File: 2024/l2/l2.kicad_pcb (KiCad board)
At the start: 2 copper layers, 175 x 169.4 mm, 45 parts, among them J1 Conn_01x04, J2 Conn_01x02, J3 Conn_01x04, Q1 IRF540N, Q2 IRF540N, Q3 IRF540N, Q4 IRF540N, SW1 SW_SPDT, U1 VNH5019A-E, U2 VNH5019A-E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

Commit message: 16/8 final
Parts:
- added H1: MountingHole_Pad, MountingHole:MountingHole_3.2mm_M3_Pad_Via, F.Cu at (245.0, 118.0)
- added H10: MountingHole_Pad, MountingHole:MountingHole_3.2mm_M3_Pad_Via, F.Cu at (260.9, 126.0)
- added H11: MountingHole_Pad, MountingHole:MountingHole_3.2mm_M3_Pad_Via, F.Cu at (260.9, 133.9)
- added H12: MountingHole_Pad, MountingHole:MountingHole_3.2mm_M3_Pad_Via, F.Cu at (260.9, 141.9)
- added H13: MountingHole_Pad, MountingHole:MountingHole_3.2mm_M3_Pad_Via, F.Cu at (268.8, 118.0)
- added H14: MountingHole_Pad, MountingHole:MountingHole_3.2mm_M3_Pad_Via, F.Cu at (268.8, 126.0)
- added H15: MountingHole_Pad, MountingHole:MountingHole_3.2mm_M3_Pad_Via, F.Cu at (268.8, 133.9)
- added H16: MountingHole_Pad, MountingHole:MountingHole_3.2mm_M3_Pad_Via, F.Cu at (268.8, 141.9)
- added H2: MountingHole_Pad, MountingHole:MountingHole_3.2mm_M3_Pad_Via, F.Cu at (245.0, 126.0)
- added H3: MountingHole_Pad, MountingHole:MountingHole_3.2mm_M3_Pad_Via, F.Cu at (245.0, 133.9)
- added H4: MountingHole_Pad, MountingHole:MountingHole_3.2mm_M3_Pad_Via, F.Cu at (245.0, 141.9)
- added H5: MountingHole_Pad, MountingHole:MountingHole_3.2mm_M3_Pad_Via, F.Cu at (252.9, 118.0)
- added H6: MountingHole_Pad, MountingHole:MountingHole_3.2mm_M3_Pad_Via, F.Cu at (252.9, 126.0)
- added H7: MountingHole_Pad, MountingHole:MountingHole_3.2mm_M3_Pad_Via, F.Cu at (252.9, 133.9)
- added H8: MountingHole_Pad, MountingHole:MountingHole_3.2mm_M3_Pad_Via, F.Cu at (252.9, 141.9)
- added H9: MountingHole_Pad, MountingHole:MountingHole_3.2mm_M3_Pad_Via, F.Cu at (260.9, 118.0)
- C1, C2, C3, C4: footprint Capacitor_SMD:C_0603_1608Metric_Pad1.08x0.95mm_HandSolder -> Capacitor_THT:CP_Radial_D8.0mm_P3.50mm
- moved R8 16.8 mm to (168.7, 95.7), turned to 180 degrees
- moved R12 9.37 mm to (169.9, 98.2)
- moved R11 7.68 mm to (168.8, 94.0)
- moved R10 6.78 mm to (168.9, 90.7)
- moved R13 4.12 mm to (173.8, 89.9)
- moved R14 2.06 mm to (168.7, 92.4), turned to 180 degrees
- turned U1 to 180 degrees
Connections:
- R14 pad 1: /Motor Driver/PWM_1 -> PWM_1
- U5 pad 4: /PWM_1 -> PWM_1
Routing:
- net /Motor Driver/MD: track 0.00 -> 3.96 mm
- net Net-(U1-EN/DIAGB): track 0.00 -> 3.76 mm
- net Net-(U1-PWM): track 0.00 -> 3.66 mm

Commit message: 21/8 final
about 10% done l2 pcb
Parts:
- added J4: Conn_01x02, Connector_AMASS:AMASS_XT30UPB-F_1x02_P5.0mm_Vertical, F.Cu at (144.6, 97.0)
- added J5: Conn_01x02, Connector_AMASS:AMASS_XT30UPB-F_1x02_P5.0mm_Vertical, F.Cu at (190.2, 54.5)
- added J6: Conn_01x02, Connector_AMASS:AMASS_XT30UPB-F_1x02_P5.0mm_Vertical, F.Cu at (295.0, 78.4)
- added J7: Conn_01x02, Connector_AMASS:AMASS_XT30UPB-F_1x02_P5.0mm_Vertical, F.Cu at (295.0, 85.7)
- moved H1 136.5 mm to (125.1, 52.6)
- moved U5 67.3 mm to (319.1, 108.3)
- moved Q1 40.6 mm to (197.9, 75.4)
- moved C1 38.4 mm to (170.3, 123.8)
- moved R12 31.6 mm to (141.1, 85.3), turned to 90 degrees
- moved R8 27.9 mm to (142.8, 85.4), turned to 90 degrees
- moved R11 25.8 mm to (144.5, 85.4), turned to -90 degrees
- moved R14 23.7 mm to (146.1, 85.3), turned to 90 degrees
- moved R13 23.3 mm to (150.9, 85.6), turned to 90 degrees
- moved U1 21.9 mm to (146.5, 71.9), turned to 90 degrees
- moved R10 21.7 mm to (147.9, 85.5), turned to -90 degrees
- moved R9 21.0 mm to (149.4, 85.6), turned to 90 degrees
- moved J2 3.28 mm to (273.4, 64.8)
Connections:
- R12 pad 1: /Motor Driver/INA_1 -> INA_1
- R13 pad 1: /Motor Driver/INB_1 -> INB_1
- R19 pad 1: /Motor Driver/INA_3 -> INA_3
- R20 pad 1: /Motor Driver/INB_3 -> INB_3
- R21 pad 1: /Motor Driver/PWM_3 -> PWM_3
- R26 pad 1: /Motor Driver/INA_4 -> INA_4
- R27 pad 1: /Motor Driver/INB_4 -> INB_4
- R28 pad 1: /Motor Driver/PWM_4 -> PWM_4
- R5 pad 1: /Motor Driver/INA_2 -> INA_2
- R6 pad 1: /Motor Driver/INB_2 -> INB_2
- R7 pad 1: /Motor Driver/PWM_2 -> PWM_2
- U5 pad 10: /INA_3 -> INA_3
- U5 pad 11: /INB_3 -> INB_3
- U5 pad 12: /PWM_3 -> PWM_3
- U5 pad 13: /INA_3 -> INA_4
- U5 pad 14: /INB_3 -> INB_4
- U5 pad 15: /PWM_3 -> PWM_4
- U5 pad 2: /INA_1 -> INA_1
- U5 pad 3: /INB_1 -> INB_1
- U5 pad 5: /INA_2 -> INA_2
- U5 pad 6: /INB_2 -> INB_2
- U5 pad 9: /PWM_2 -> PWM_2
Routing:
- net Net-(J4-Pin_1): track 0.00 -> 18.1 mm
- net Net-(J4-Pin_2): track 0.00 -> 17.7 mm
- net Net-(U1-EN/DIAGA): track 0.00 -> 5.44 mm
- net Net-(U1-INB): track 0.00 -> 4.72 mm
- net Net-(U1-INA): track 0.00 -> 4.01 mm
- net /Motor Driver/MD: track 3.96 -> 6.76 mm
- net Net-(U1-EN/DIAGB): track 3.76 -> 5.34 mm

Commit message: 28/8 final
resistors for motor driver removed as it was too cumbersome to do the traces and is also completely optional
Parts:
- removed R1, R12, R13, R14, R15, R16, R19, R2, R20, R21, R22, R23, R26, R27, R28, R5, R6, R7, R8, R9: 1k, Resistor_SMD:R_0603_1608Metric_Pad0.98x0.95mm_HandSolder
- removed R10, R11, R17, R18, R24, R25, R3, R4: 3.3k, Resistor_SMD:R_0603_1608Metric_Pad0.98x0.95mm_HandSolder
- J4, J5, J6, J7: moved to B.Cu
- moved U5 277.1 mm to (42.1, 101.3), turned to 180 degrees
- moved H14 243.2 mm to (29.8, 81.3)
- moved H13 239.1 mm to (29.8, 123.3)
- moved J6 234.0 mm to (69.0, 139.2)
- moved H15 220.2 mm to (55.0, 81.2)
- moved H16 209.6 mm to (79.5, 52.1)
- moved H12 206.7 mm to (55.0, 123.4)
- moved H10 191.6 mm to (76.3, 177.2)
- moved H11 182.4 mm to (79.5, 152.6)
- moved J7 163.3 mm to (143.1, 145.6)
- moved C3 157.4 mm to (82.3, 139.3)
- moved Q3 154.2 mm to (88.6, 130.8)
- moved U2 147.9 mm to (73.2, 72.5), turned to 90 degrees
- moved Q2 147.6 mm to (86.5, 83.7)
- moved C2 146.3 mm to (86.5, 92.0), turned to 180 degrees
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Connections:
- SW1 pad 2: /Motor Driver/MD -> GND
- U1 pad 10: Net-(U1-INB) -> INB_1
- U1 pad 4: Net-(U1-INA) -> INA_1
- U1 pad 5: Net-(U1-EN/DIAGA) -> GND
- U1 pad 7: Net-(U1-PWM) -> PWM_1
- U1 pad 9: Net-(U1-EN/DIAGB) -> GND
- U2 pad 10: Net-(U2-INB) -> INB_2
- U2 pad 4: Net-(U2-INA) -> INA_2
- U2 pad 5: Net-(U2-EN/DIAGA) -> GND
- U2 pad 7: Net-(U2-PWM) -> PWM_2
- U2 pad 9: Net-(U2-EN/DIAGB) -> GND
- U3 pad 10: Net-(U3-INB) -> INB_3
- U3 pad 4: Net-(U3-INA) -> INA_3
- U3 pad 5: Net-(U3-EN/DIAGA) -> GND
- U3 pad 7: Net-(U3-PWM) -> PWM_3
- U3 pad 9: Net-(U3-EN/DIAGB) -> GND
- U4 pad 10: Net-(U4-INB) -> INB_4
- U4 pad 4: Net-(U4-INA) -> INA_4
- U4 pad 5: Net-(U4-EN/DIAGA) -> GND
- U4 pad 7: Net-(U4-PWM) -> PWM_4
- U4 pad 9: Net-(U4-EN/DIAGB) -> GND
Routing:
- net Net-(J4-Pin_1): track 18.1 -> 0.00 mm
- net Net-(J4-Pin_2): track 17.7 -> 0.00 mm
- net /Motor Driver/MD: track 6.76 -> 0.00 mm
- net Net-(U1-EN/DIAGA): track 5.44 -> 0.00 mm
- net Net-(U1-EN/DIAGB): track 5.34 -> 0.00 mm
- net Net-(U1-INB): track 4.72 -> 0.00 mm
- net Net-(U1-INA): track 4.01 -> 0.00 mm
- net Net-(U1-PWM): track 3.66 -> 0.00 mm

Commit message: 4/9 final
some cursed motor driver routing
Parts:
- moved U5 186.0 mm to (222.7, 146.3)
- moved C3 184.0 mm to (263.9, 168.9)
- moved J6 184.0 mm to (250.7, 168.8)
- moved Q3 184.0 mm to (270.2, 160.4)
- moved U3 184.0 mm to (254.5, 147.5)
- moved C2 156.5 mm to (234.9, 42.3)
- moved J5 156.5 mm to (219.0, 37.4)
- moved U2 156.5 mm to (221.6, 22.9)
- moved Q2 156.5 mm to (234.9, 34.0)
- moved J7 107.6 mm to (227.3, 78.6)
- moved C4 107.6 mm to (240.8, 78.2)
- moved Q4 107.6 mm to (253.3, 47.9)
- moved U4 107.6 mm to (231.8, 60.7)
- moved J4 34.1 mm to (121.4, 71.3), turned to 45 degrees
- moved C1 29.4 mm to (162.3, 67.8), turned to -45 degrees
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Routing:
- net GND: track 0.00 -> 6.83 mm, vias 0 -> 2
- net /Motor Driver/CP: track 0.00 -> 0.51 mm
- added copper zone on F.Cu, net +5V
- added copper zone on F.Cu, net Net-(J4-Pin_1)
- added copper zone on F.Cu, net Net-(J4-Pin_2)

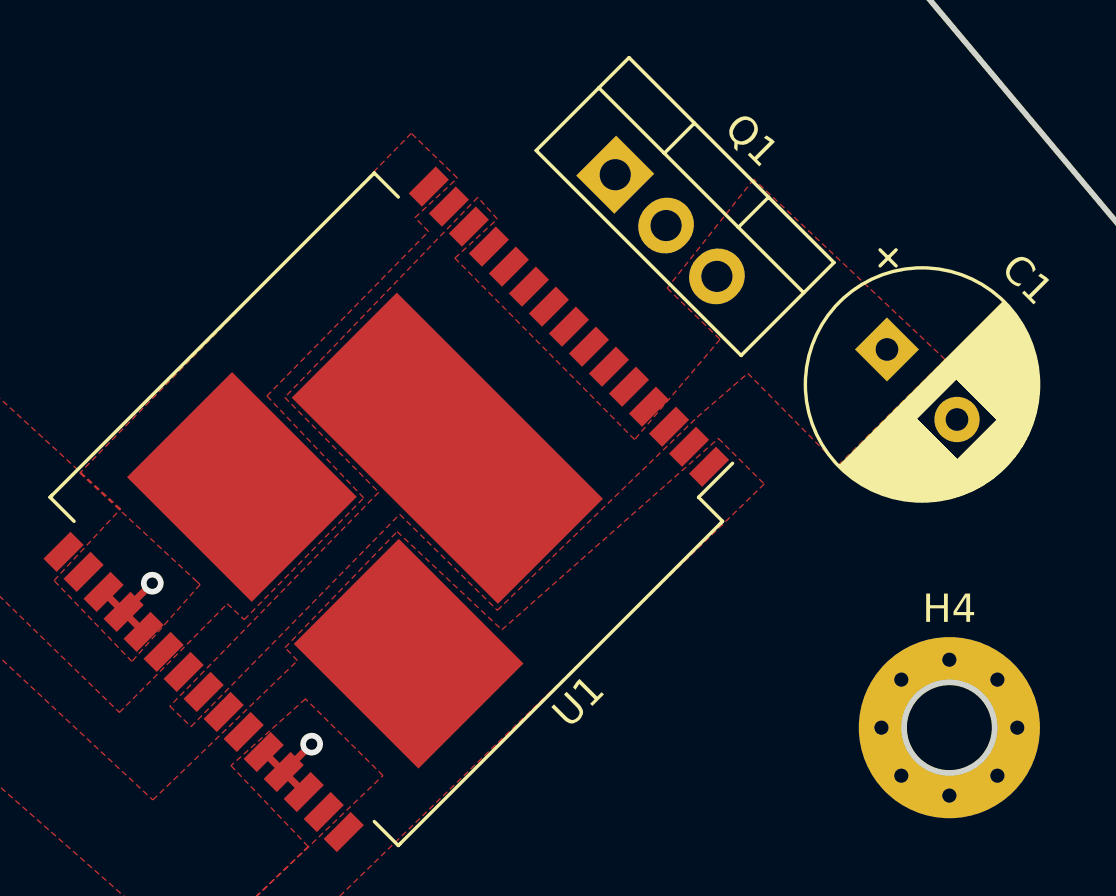
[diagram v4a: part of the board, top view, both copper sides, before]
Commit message: 5/9 final
fixed the problem with motor driver schematics
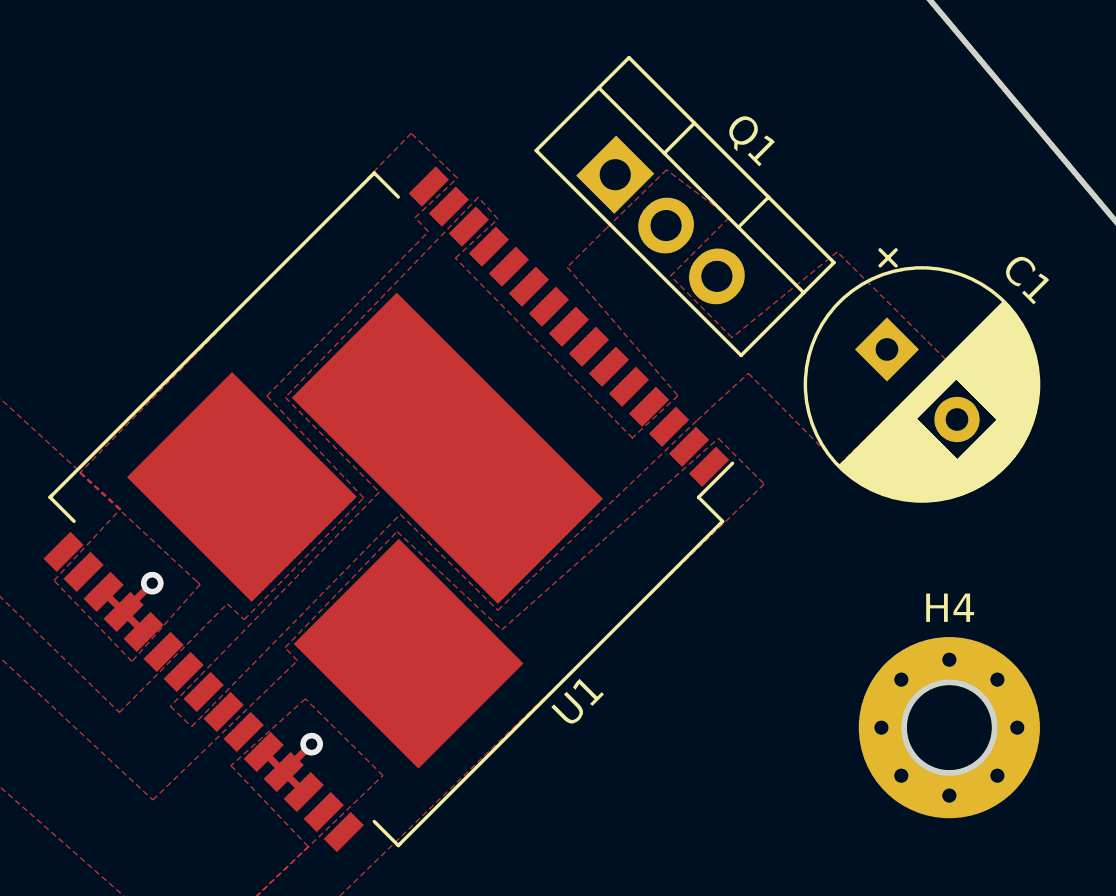
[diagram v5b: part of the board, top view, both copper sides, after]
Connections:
- C1 pad 1: +5V -> Net-(Q1-D)
- C2 pad 1: +5V -> Net-(Q2-D)
- C3 pad 1: +5V -> Net-(Q3-D)
- C4 pad 1: +5V -> Net-(Q4-D)
- Q1 pad 1: /Motor Driver/CP -> /Motor Driver/CP1
- Q1 pad 2: +12V -> Net-(Q1-D)
- Q1 pad 3: +5V -> +12V
- Q2 pad 1: /Motor Driver/CP -> /Motor Driver/CP2
- Q2 pad 2: +12V -> Net-(Q2-D)
- Q2 pad 3: +5V -> +12V
- Q3 pad 1: /Motor Driver/CP -> /Motor Driver/CP3
- Q3 pad 2: +12V -> Net-(Q3-D)
- Q3 pad 3: +5V -> +12V
- Q4 pad 1: /Motor Driver/CP -> /Motor Driver/CP4
- Q4 pad 2: +12V -> Net-(Q4-D)
- Q4 pad 3: +5V -> +12V
- SW1 pad 2: GND -> /Motor Driver/MD
- U1 pad 11: /Motor Driver/CP -> /Motor Driver/CP1
- U1 pad 13: +5V -> Net-(Q1-D)
- U1 pad 23: +5V -> Net-(Q1-D)
- U1 pad 3: +5V -> Net-(Q1-D)
- U1 pad 31: +5V -> Net-(Q1-D)
- U1 pad 5: GND -> /Motor Driver/MD
- U1 pad 9: GND -> /Motor Driver/MD
- U2 pad 11: /Motor Driver/CP -> /Motor Driver/CP2
- U2 pad 13: +5V -> Net-(Q2-D)
- U2 pad 23: +5V -> Net-(Q2-D)
- U2 pad 3: +5V -> Net-(Q2-D)
- U2 pad 31: +5V -> Net-(Q2-D)
- U2 pad 5: GND -> /Motor Driver/MD
- U2 pad 9: GND -> /Motor Driver/MD
- U3 pad 11: /Motor Driver/CP -> /Motor Driver/CP3
- U3 pad 13: +5V -> Net-(Q3-D)
- U3 pad 23: +5V -> Net-(Q3-D)
- U3 pad 3: +5V -> Net-(Q3-D)
- U3 pad 31: +5V -> Net-(Q3-D)
- U3 pad 5: GND -> /Motor Driver/MD
- U3 pad 9: GND -> /Motor Driver/MD
- U4 pad 11: /Motor Driver/CP -> /Motor Driver/CP4
- U4 pad 13: +5V -> Net-(Q4-D)
- U4 pad 23: +5V -> Net-(Q4-D)
- U4 pad 3: +5V -> Net-(Q4-D)
- U4 pad 31: +5V -> Net-(Q4-D)
- U4 pad 5: GND -> /Motor Driver/MD
- U4 pad 9: GND -> /Motor Driver/MD
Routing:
- net /Motor Driver/CP1: track 0.00 -> 0.51 mm
- net /Motor Driver/CP: track 0.51 -> 0.00 mm

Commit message: edited motor driver pcb
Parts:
- moved U5 129.8 mm to (301.6, 43.2)
- moved J2 94.2 mm to (188.3, 105.2), turned to 90 degrees
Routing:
- net +12V: track 0.00 -> 176.9 mm
- net /Motor Driver/MD: track 0.00 -> 5.94 mm
- net /Motor Driver/CP1: track 0.51 -> 5.10 mm
- added copper zone on F.Cu, net +12V
- added copper zone on F.Cu, net Net-(Q1-D)
- removed copper zone on F.Cu, net +5V
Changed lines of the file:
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@@
 	(footprint "Connector_AMASS:AMASS_XT60-M_1x02_P7.20mm_Vertical"
 		(layer "F.Cu")
-		(at 273.43 64.84)
+		(at 188.32 105.16 90)
 		(descr "AMASS female XT60, through hole, vertical, https://www.tme.eu/Document/2d152ced3b7a446066e6c419d84bb460/XT60%20SPEC.pdf")
 		(tags "XT60 female vertical")
 		(property "Reference" "J2"
-			(at 3.6 -5.3 180)
+			(at 3.599999 -5.3 90)
 			(layer "F.SilkS")
 			(effects
@@
 		)
 		(property "Value" "Conn_01x02"
-			(at 3.6 5.4 0)
+			(at 3.6 5.4 90)
 			(layer "F.Fab")
 			(effects
@@
 		)
 		(property "Footprint" "Connector_AMASS:AMASS_XT60-M_1x02_P7.20mm_Vertical"
-			(at 0 0 0)
+			(at 0 0 90)
 			(layer "F.Fab")
 			(hide yes)
@@
 		)
 		(property "Datasheet" ""
-			(at 0 0 0)
+			(at 0 0 90)
 			(layer "F.Fab")
 			(hide yes)
@@
 		)
 		(property "Description" ""
-			(at 0 0 0)
+			(at 0 0 90)
 			(layer "F.Fab")
 			(hide yes)
@@
 		(attr through_hole)
 		(fp_line
-			(start -4.25 -1.6)
-			(end -4.25 1.55)
+			(start -1.4 -4.150001)
+			(end -4.25 -1.6)
 			(stroke
 				(width 0.12)
@@
 		)
 		(fp_line
-			(start -4.25 1.55)
-			(end -1.4 4.15)
+			(start 11.450001 -4.15)
+			(end -1.4 -4.150001)
 			(stroke
 				(width 0.12)
@@
 		)
 		(fp_line
-			(start -1.4 -4.15)
-			(end -4.25 -1.6)
+			(start -4.25 -1.6)
+			(end -4.25 1.55)
 			(stroke
 				(width 0.12)
@@
 		)
 		(fp_line
-			(start -1.4 4.15)
-			(end 11.45 4.15)
+			(start -4.25 1.55)
+			(end -1.4 4.150001)
 			(stroke
 				(width 0.12)
@@
 		)
 		(fp_line
-			(start 11.45 -4.15)
-			(end -1.4 -4.15)
+			(start 11.450001 4.15)
+			(end 11.450001 -4.15)
 			(stroke
 				(width 0.12)
@@
 		)
 		(fp_line
-			(start 11.45 4.15)
-			(end 11.45 -4.15)
+			(start -1.4 4.150001)
+			(end 11.450001 4.15)
 			(stroke
 				(width 0.12)
@@
 		)
 		(fp_line
-			(start -4.65 -1.85)
-			(end -1.6 -4.6)
+			(start 11.85 -4.6)
+			(end 11.85 4.6)
 			(stroke
 				(width 0.05)
@@
 		)
 		(fp_line
-			(start -4.65 1.85)
-			(end -4.65 -1.85)
+			(start -1.6 -4.6)
+			(end 11.85 -4.6)
 			(stroke
 				(width 0.05)
@@
 		)
 		(fp_line
-			(start -1.6 -4.6)
-			(end 11.85 -4.6)
+			(start -4.65 -1.85)
+			(end -1.6 -4.6)
 			(stroke
 				(width 0.05)
@@
 		)
 		(fp_line
-			(start -1.6 4.6)
-			(end -4.65 1.85)
+			(start -4.65 1.85)
+			(end -4.65 -1.85)
 			(stroke
 				(width 0.05)
@@
 		)
 		(fp_line
-			(start 11.85 -4.6)
-			(end 11.85 4.6)
+			(start 11.85 4.6)
+			(end -1.6 4.6)
 			(stroke
 				(width 0.05)
@@
 		)
 		(fp_line
-			(start 11.85 4.6)
-			(end -1.6 4.6)
+			(start -1.6 4.6)
+			(end -4.65 1.85)
 			(stroke
 				(width 0.05)
@@
 		)
 		(fp_line
-			(start -4.15 -1.55)
-			(end -4.15 1.55)
+			(start -1.4 -4.05)
+			(end -4.150001 -1.55)
 			(stroke
 				(width 0.12)
@@
 		)
 		(fp_line
-			(start -4.15 1.55)
-			(end -1.4 4.05)
+			(start 11.35 -4.049999)
+			(end -1.4 -4.05)
 			(stroke
 				(width 0.12)
@@
 		)
 		(fp_line
-			(start -1.4 -4.05)
-			(end -4.15 -1.55)
+			(start -4.150001 -1.55)
+			(end -4.150001 1.55)
 			(stroke
 				(width 0.12)
@@
 		)
 		(fp_line
-			(start -1.4 4.05)
-			(end 11.35 4.05)
+			(start -4.150001 1.55)
+			(end -1.4 4.05)
 			(stroke
 				(width 0.12)
@@
 		)
 		(fp_line
-			(start 11.35 -4.05)
-			(end -1.4 -4.05)
+			(start 11.35 4.049999)
+			(end 11.35 -4.049999)
 			(stroke
 				(width 0.12)
@@
 		)
 		(fp_line
-			(start 11.35 4.05)
-			(end 11.35 -4.05)
+			(start -1.4 4.05)
+			(end 11.35 4.049999)
 			(stroke
 				(width 0.12)
@@
 		)
 		(fp_text user "${REFERENCE}"
-			(at 3.6 0.05 0)
+			(at 3.6 0.05 90)
 			(layer "F.Fab")
 			(effects
@@
 		)
 		(pad "1" thru_hole roundrect
-			(at 0 0)
+			(at 0 0 90)
 			(size 6 6)
 			(drill 4.5)
@@
 		)
 		(pad "2" thru_hole circle
-			(at 7.2 0)
+			(at 7.2 0 90)
 			(size 6 6)
 			(drill 4.5)
@@
 	(footprint "Board:MODULE_DEV-15583"
 		(layer "F.Cu")
-		(at 222.68 146.26 180)
+		(at 301.64 43.25 180)
 		(property "Reference" "U5"
 			(at -5.715 -19.685 0)
@@
 	)
 	(segment
+		(start 154.23 59.43)
+		(end 154.68 59.43)
+		(width 0.4)
+		(layer "F.Cu")
+		(net 5)
+	)
+	(segment
+		(start 188.32 97.96)
+		(end 111.99 97.96)
+		(width 0.4)
+		(layer "F.Cu")
+		(net 5)
+	)
+	(segment
+		(start 153.02 59.43)
+		(end 154.23 59.43)
+		(width 0.4)
+		(layer "F.Cu")
+		(net 5)
+	)
+	(segment
+		(start 151.83 59.43)
+		(end 153.02 59.43)
+		(width 0.25)
+		(layer "F.Cu")
+		(net 5)
+	)
+	(segment
+		(start 154.23 59.43)
+		(end 151.74 59.43)
+		(width 0.4)
+		(layer "F.Cu")
+		(net 5)
+	)
+	(segment
+		(start 148.86 62.31)
+		(end 148.86 63.58365)
+		(width 0.4)
+		(layer "F.Cu")
+		(net 5)
+	)
+	(segment
+		(start 114.78 59.43)
+		(end 153.02 59.43)
+		(width 0.4)
+		(layer "F.Cu")
+		(net 5)
+	)
+	(segment
+		(start 107.12 67.09)
+		(end 114.78 59.43)
+		(width 0.4)
+		(layer "F.Cu")
+		(net 5)
+	)
+	(segment
+		(start 151.74 59.43)
+		(end 148.86 62.31)
+		(width 0.4)
+		(layer "F.Cu")
+		(net 5)
+	)
+	(segment
+		(start 148.86 63.58365)
+		(end 148.231825 64.211825)
+		(width 0.4)
+		(layer "F.Cu")
+		(net 5)
+	)
+	(segment
+		(start 111.99 97.96)
+		(end 107.12 93.09)
+		(width 0.4)
+		(layer "F.Cu")
+		(net 5)
+	)
+	(segment
+		(start 156.85 64.702102)
+		(end 156.85 61.6)
+		(width 0.4)
+		(layer "F.Cu")
+		(net 5)
+	)
+	(segment
+		(start 156.85 61.6)
+		(end 154.68 59.43)
+		(width 0.4)
+		(layer "F.Cu")
+		(net 5)
+	)
+	(segment
+		(start 107.12 93.09)
+		(end 107.12 67.09)
+		(width 0.4)
+		(layer "F.Cu")
+		(net 5)
+	)
+	(segment
+		(start 156.287835 65.264267)
+		(end 156.85 64.702102)
+		(width 0.4)
+		(layer "F.Cu")
+		(net 5)
+	)
+	(segment
+		(start 148.231825 64.211825)
+		(end 148.231825 64.118175)
+		(width 0.25)
+		(layer "F.Cu")
+		(net 5)
+	)
+	(segment
+		(start 152.695733 61.672165)
+		(end 152.185699 61.672165)
+		(width 0.25)
+		(layer "F.Cu")
+		(net 222)
+	)
+	(segment
 		(start 152.185699 61.672165)
-		(end 152.695733 61.672165)
+		(end 148.938932 64.918932)
 		(width 0.25)
 		(layer "F.Cu")
 		(net 222)
 	)
+	(segment
+		(start 152.704276 69.63887)
+		(end 151.58887 69.63887)
+		(width 0.25)
+		(layer "F.Cu")
+		(net 226)
+	)
+	(segment
+		(start 151.58887 69.63887)
+		(end 149.95 68)
+		(width 0.25)
+		(layer "F.Cu")
+		(net 226)
+	)
+	(segment
+		(start 149.95 66.736292)
+		(end 150.353146 66.333146)
+		(width 0.25)
+		(layer "F.Cu")
+		(net 226)
+	)
+	(segment
+		(start 153.181573 69.161573)
+		(end 152.704276 69.63887)
+		(width 0.25)
+		(layer "F.Cu")
+		(net 226)
+	)
+	(segment
+		(start 149.95 68)
+		(end 149.95 66.736292)
+		(width 0.25)
+		(layer "F.Cu")
+		(net 226)
+	)
 	(zone
 		(net 19)
@@
 	)
 	(zone
-		(net 2)
-		(net_name "+5V")
+		(net 8)
+		(net_name "Net-(Q1-D)")
 		(layer "F.Cu")
 		(hatch none 0.5)
@@
 				(xy 137.73 81.17) (xy 145.1 73.67) (xy 148.55 77.06) (xy 155.59 70.35) (xy 157.4 68.69) (xy 160.6 71.93)
 				(xy 164.37 68.2) (xy 160.54 64.4) (xy 156.82 67.43) (xy 154.65 65.25) (xy 156.73 63.18) (xy 154.51 61.5)
-				(xy 152.41 63.54) (xy 151 64.94) (xy 154.91 69.48) (xy 153.29 70.98) (xy 153.31 70.98) (xy 147.05 64.62)
+				(xy 152.41 63.54) (xy 151 64.94) (xy 154.91 69.48) (xy 153.29 70.98) (xy 152.47 71.97) (xy 146.24 65.71)
 				(xy 148.55 63.24) (xy 147.86 62.47) (xy 141.04 69.54) (xy 144.36 72.89) (xy 136.98 80.45)
 			)
 		)
+	)
+	(zone
+		(net 5)
+		(net_name "+12V")
+		(layer "F.Cu")
+		(hatch edge 0.5)
+		(priority 4)
+		(connect_pads yes
+			(clearance 0.2)
+		)
+		(min_thickness 0.2)
+		(filled_areas_thickness no)
+		(fill yes
+			(thermal_gap 0.5)
+			(thermal_bridge_width 0.5)
+			(smoothing fillet)
+			(radius 0.5)
+		)
+		(polygon
+			(pts
+				(xy 193.97 101.39) (xy 194.1 93.11) (xy 115.5 91.28) (xy 115.64 49.43) (xy 93.46 50.13) (xy 93.08 91.22)
+				(xy 42.8 91.22) (xy 42.96 113.61) (xy 177.26 113.61) (xy 177.21 101.35)
+			)
+		)
